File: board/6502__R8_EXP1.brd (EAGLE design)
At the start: 140.9 x 91.1 mm, 19 parts, among them IC2 74HCT02N, IC3 74HCT04N, IC4 74HCT373N, IC5 74HCT02N, IC6 74HCT244N

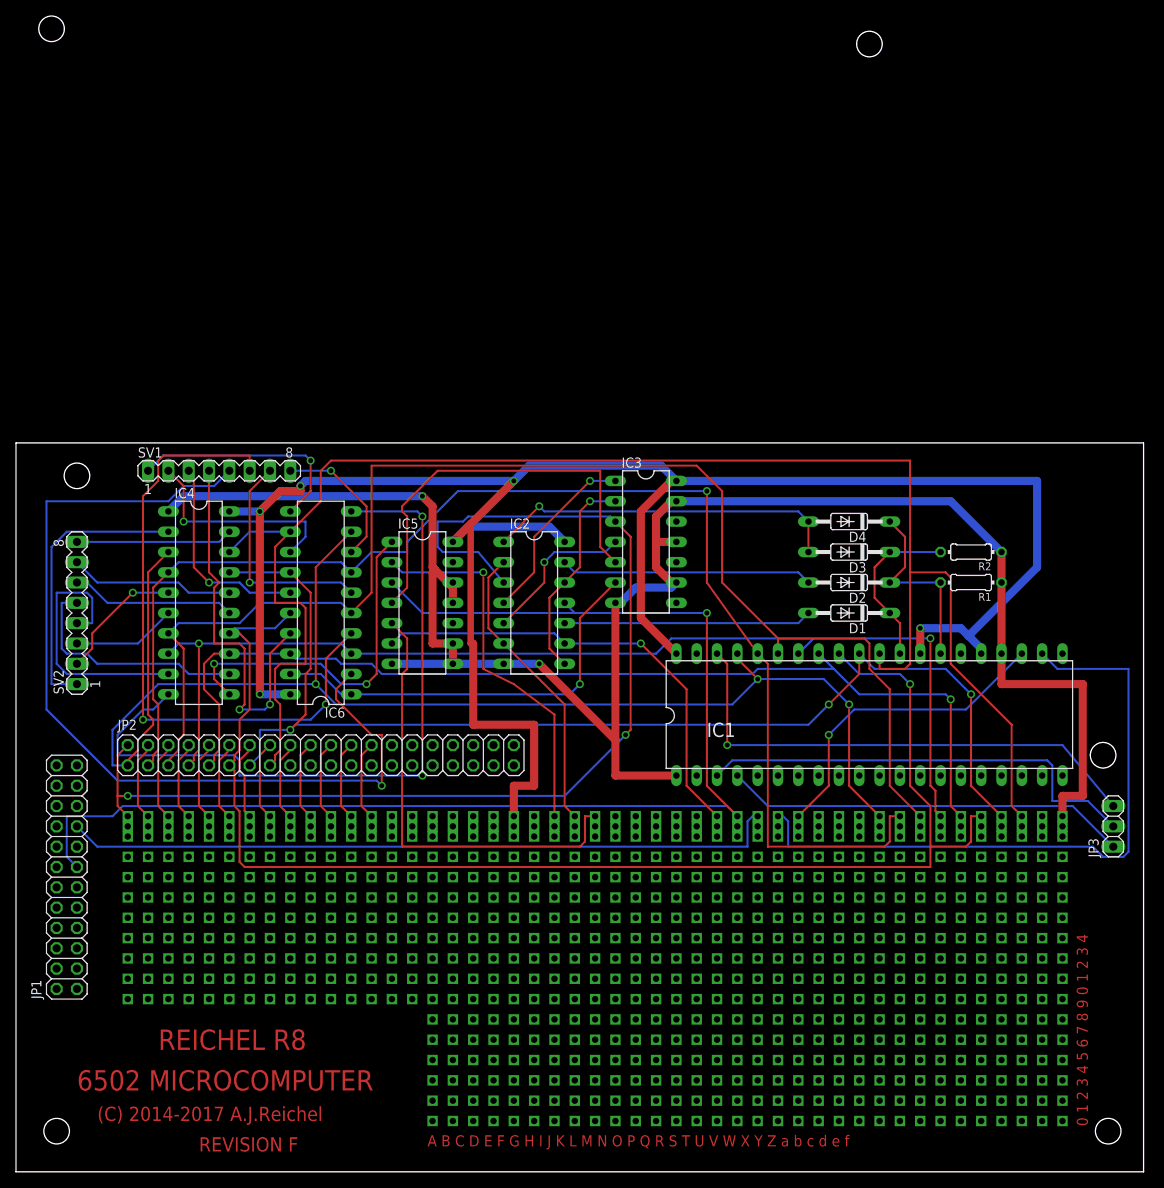
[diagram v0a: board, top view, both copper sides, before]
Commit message: Expansion board: Improve Layout, Fix Errors
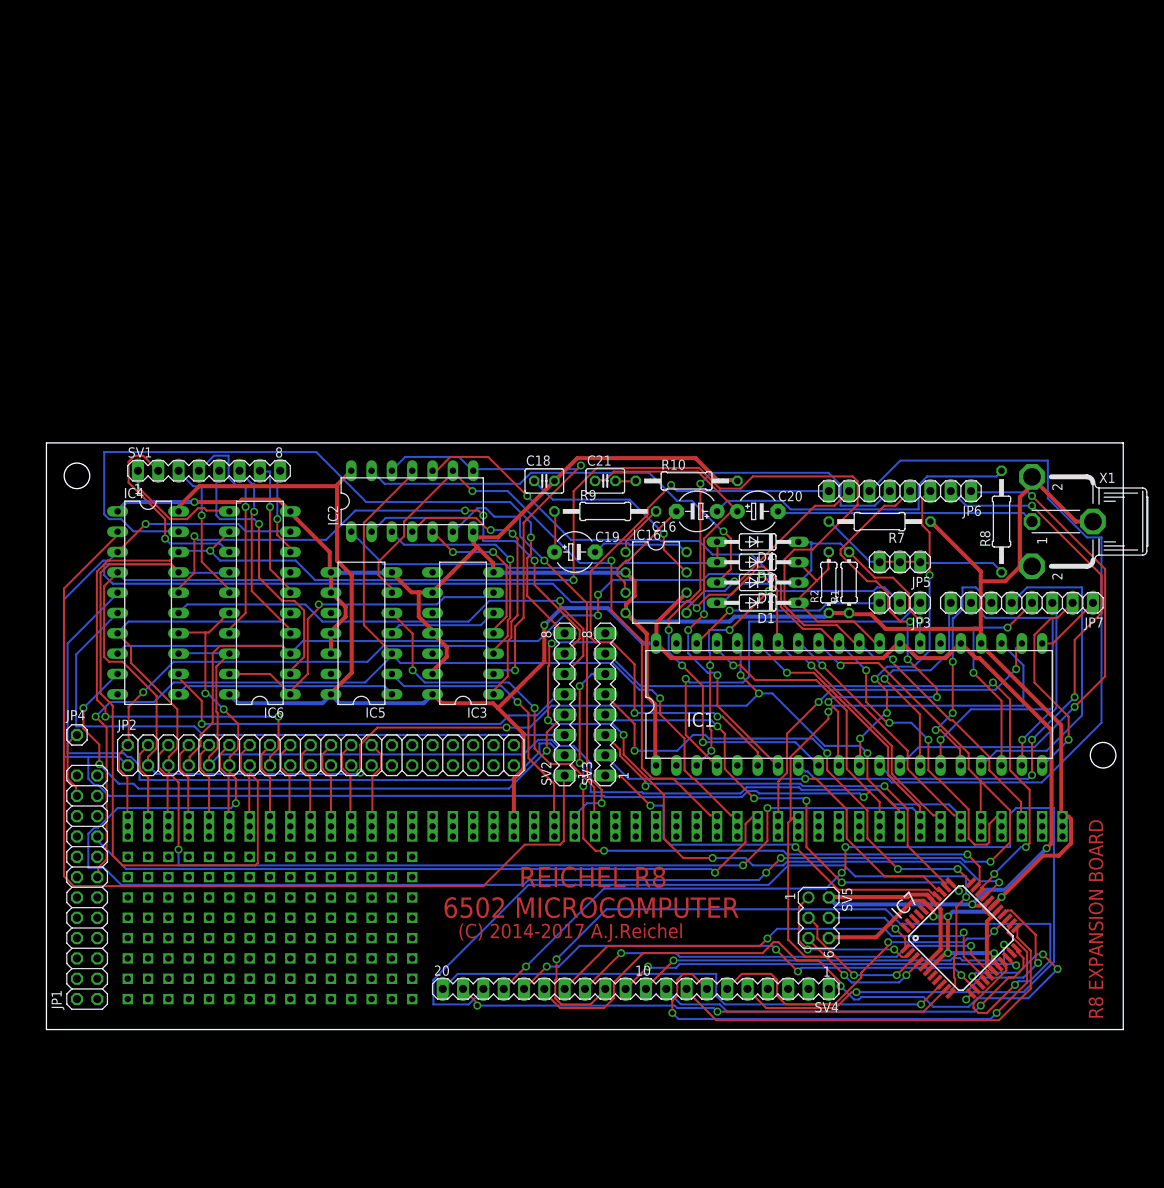
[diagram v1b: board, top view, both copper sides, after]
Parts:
- added C16: 1u, rcl:E5-5
- added C18: 100n, rcl:C025-030X050
- added C19: 10u, rcl:E5-5
- added C20: 220u, rcl:E5-5
- added C21: 47n, rcl:C025-030X050
- added IC16: LM386N-3, linear:DIL08
- added IC7: MEGA32-A, atmel:TQFP44
- added JP4: (no value), pinhead:1X01
- added JP5: (no value), pinhead:1X03
- added JP6, JP7: (no value), pinhead:1X08
- added R10: 10R, rcl:0207/12
- added R7: 1k, rcl:0207/12
- added R8: 10k, rcl:0207/12
- added R9: 1k2, rcl:0207/12
- added SV3: (no value), con-lstb:MA08-1
- added SV4: (no value), con-lstb:MA20-1
- added SV5: (no value), con-lstb:MA03-2
- added X1: TOBU3, logik2:TOBU3
- U$2: device logik:SOLDERPAD -> logik2:SOLDERPAD
- moved SV2 62.0 mm to (59.7, 7.62)
- moved JP3 38.6 mm to (101.6, 20.3), turned to 180 degrees
- moved IC3 25.6 mm to (47.0, 16.5), turned to 90 degrees
- moved IC2 19.8 mm to (40.6, 33.0), turned to 0 degrees
- moved R2 18.2 mm to (92.7, 22.9), turned to 90 degrees
- moved R1 15.2 mm to (95.2, 22.9), turned to 90 degrees
- moved D4 11.7 mm to (83.8, 27.9)
- moved D1 11.5 mm to (83.8, 20.3)
- moved D3 11.5 mm to (83.8, 25.4)
- moved D2 11.4 mm to (83.8, 22.9)
- moved IC5 8.52 mm to (34.3, 16.5), turned to 90 degrees
- moved IC6 7.62 mm to (21.6, 20.3)
- moved IC4 6.35 mm to (7.62, 20.3)
- moved IC1 2.84 mm to (95.2, 7.62)
- moved JP1 2.84 mm to (0.00, -15.2)
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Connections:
- new net N$114: JP5.1, JP5.2, JP5.3, R7.2, R8.1
- new net N$115: C16.+, R8.2
- new net N$116: C16.-, IC16.3
- new net N$117: C18.1, IC16.7
- new net N$126: C19.-, IC16.8
- new net N$127: IC16.1, R9.2
- new net N$128: C19.+, R9.1
- new net N$129: C20.-, X1.1
- new net N$130: C20.+, C21.1, IC16.5
- new net N$133: C21.2, R10.1
- new net N$31: IC1.13, JP6.1
- new net N$32: IC7.37, SV3.1
- new net N$33: IC7.36, SV3.2
- new net N$34: IC7.35, SV3.3
- new net N$35: IC7.9, SV4.20
- new net N$36: IC7.10, SV4.19
- new net N$37: IC7.11, SV4.18
- new net N$38: IC7.12, SV4.17
- new net N$39: IC7.13, SV4.16
- new net N$40: IC7.14, SV4.15
- new net N$41: IC7.15, SV4.14
- new net N$42: IC7.16, SV4.13
- new net N$43: IC7.19, SV4.12
- new net N$44: IC7.20, SV4.11
- new net N$45: IC7.21, SV4.10
- new net N$46: IC7.22, SV4.9
- new net N$47: IC7.23, SV4.8
- new net N$48: IC7.24, SV4.7
- new net N$49: IC7.25, SV4.6
- new net N$50: IC7.26, SV4.5
- new net N$51: IC7.2, SV5.1
- new net N$52: IC7.3, SV5.3
- new net N$53: IC7.34, SV3.4
- new net N$54: IC7.1, SV5.4
- new net N$55: IC7.33, SV3.5
- new net N$56: IC7.32, SV3.6
- new net N$57: IC7.31, SV3.7
- new net N$58: IC7.30, SV3.8
- new net N$59: IC1.12, JP6.2
- new net N$60: IC1.11, JP6.3
- new net N$61: IC1.10, JP6.4
- new net N$62: IC1.9, JP6.5
- new net N$63: IC1.8, JP6.6
- new net N$64: IC1.7, JP6.7
- new net N$65: IC1.6, JP6.8
- new net N$66: IC1.21, JP7.1
- new net N$67: IC1.20, JP7.2
- new net N$68: IC1.19, JP7.3
- new net N$69: IC1.18, JP7.4
- new net N$70: IC1.17, JP7.5
- new net N$71: IC1.16, JP7.6
- new net N$72: IC1.15, JP7.7
- new net N$73: IC1.14, JP7.8
- net !RESET: now also IC7.4, SV5.5
- net !VRAM: now also JP4.1
- net GND: no longer IC6.10
- net VCC: now also IC16.6, IC7.17, IC7.27, IC7.29, IC7.38, IC7.5, SV5.2
- net VSS: now also C18.2, IC16.2, IC16.4, IC6.10, IC7.18, IC7.28, IC7.39, IC7.6, R10.2, R7.1, SV5.6, X1.2, X1.2@1, X1.2@2
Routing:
- net N$38: track 0.00 -> 115.3 mm, vias 0 -> 4
- net VSS: track 236.8 -> 346.2 mm, vias 2 -> 6
- net N$63: track 0.00 -> 102.4 mm
- net N$43: track 0.00 -> 102.2 mm, vias 0 -> 2
- net N$37: track 0.00 -> 98.9 mm, vias 0 -> 1
- net GND: track 92.8 -> 0.00 mm, vias 2 -> 0
- net N$40: track 0.00 -> 89.8 mm, vias 0 -> 4
- net D6: track 147.6 -> 237.4 mm, vias 3 -> 4
- net N$58: track 0.00 -> 89.4 mm, vias 0 -> 5
- net N$20: track 35.7 -> 119.4 mm
- net N$57: track 0.00 -> 81.4 mm, vias 0 -> 3
- net N$14: track 114.2 -> 34.4 mm
- net N$62: track 0.00 -> 79.8 mm, vias 0 -> 4
- net N$56: track 0.00 -> 77.1 mm, vias 0 -> 5
- net N$65: track 0.00 -> 75.3 mm, vias 0 -> 3
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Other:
- board size 140.9 x 91.1 mm -> 134.6 x 73.3 mm
- board text added: "R8 EXPANSION BOARD"
- board text removed: "0 1 2 3 4 5 6 7 8 9 0 1 2 3 4"
- board text removed: "A B C D E F G H I J K L M N O P Q R S T U V W X Y Z a b c d e f"
- board text removed: "REVISION F"
